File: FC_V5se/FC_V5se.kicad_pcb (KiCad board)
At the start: 4 copper layers, 88 x 94.5 mm, 220 parts, among them IC3 RV-3028-C7_32.768kHz_1ppm_TA_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, IC6 LT3652IMSE#PBF, J10 INHIBIT_P2, J11 DF11CZ-12DP-2V(27), J12 USB_C_Receptacle_USB2.0_16P, J14 Battery Input, J16 DEBUG, J17 Face4 (Z- Face), J18 Payload, J19 ISS_INHIBIT, J2 DF11CZ-12DP-2V(27), J20 RBF_Inhibit, J21 Heater Output, J22 SWD Port, J23 Aux Deploy 1, J24 Deploy 2, J29 INHIBIT_S2, J3 Life Makes Lemonade, J4 Conn_01x02, J5 BM04B-SRSS-TB(LF)(SN), J7 INHIBIT_P1, J8 INHIBIT_S1, SW1 KMR2, SW2 KMR2, U1 TLV1704, U10 TPS54226PWPRPWP14_2P31X2P46-L, U12 LT8610ABEMSE#TRPBF, U13 E22-400M30S, U14 TCA4307DGKR, U15 LIS2MDL, U16 INA219AxDCN, U19 AP22653AW6-7, U2 ZDSD04GLGEAG, U21 AP22653AW6-7, U22 AP22653AW6-7, U23 AP22653AW6-7, U24 AP22653AW6-7, U25 TPS2HB50AQPWPRQ1, U27 AP22653AW6-7, U29 AP22653AW6-7, U3 TCA9548APWR, U30 E28-2G4M27S, U6 TPS4H160AQPWPRQ1, U7 LSM6DSOTR, U8 INA219AxDCN

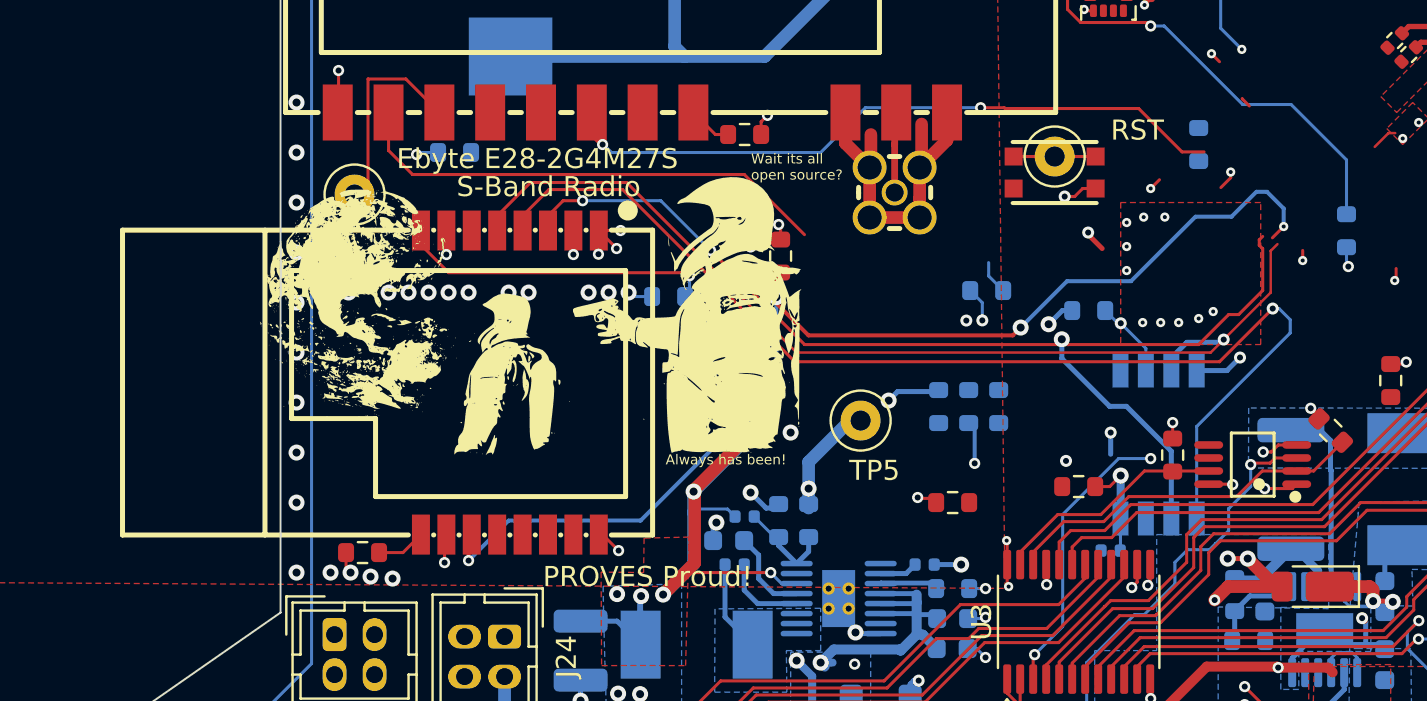
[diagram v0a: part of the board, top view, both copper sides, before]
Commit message: V5se: Deleted E28 S-Band Radio
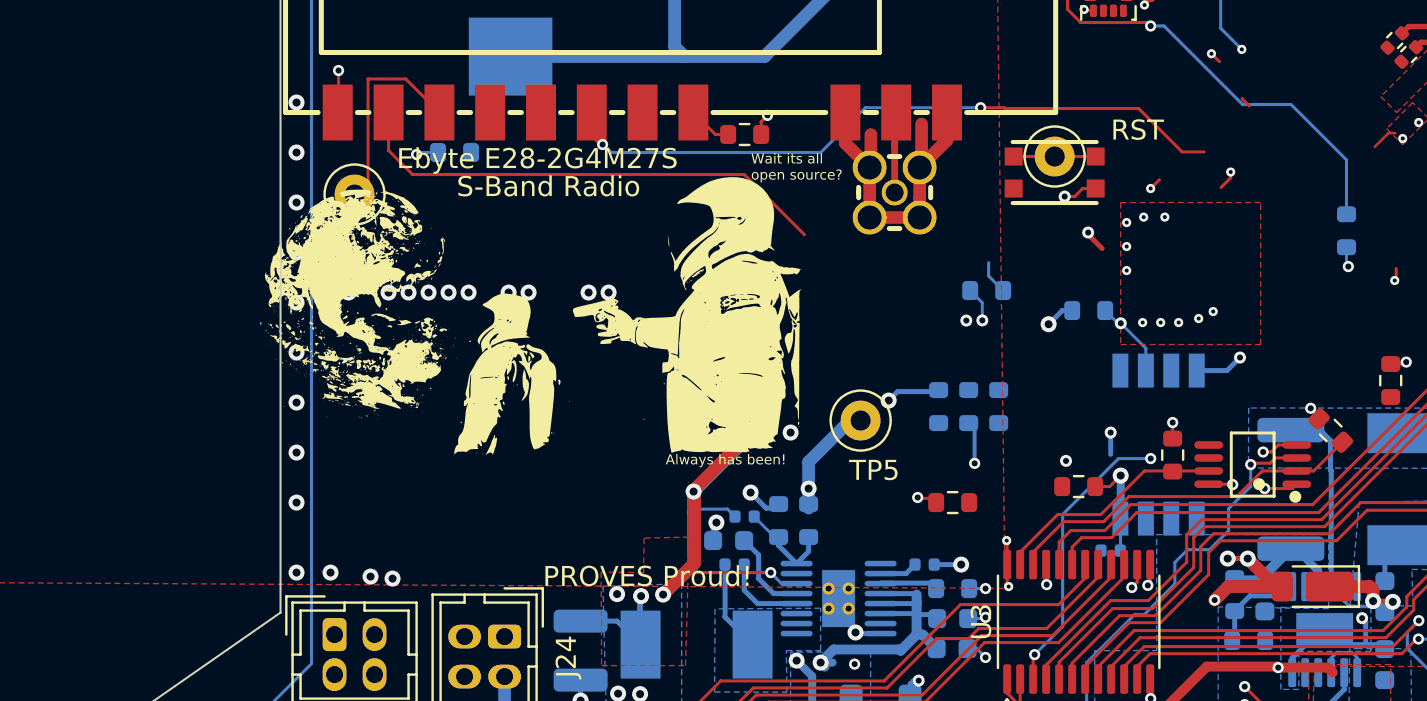
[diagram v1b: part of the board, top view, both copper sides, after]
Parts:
- removed R90: 10k, Resistor_SMD:R_0603_1608Metric
- removed R92, R95, R96: 100k, Resistor_SMD:R_0603_1608Metric
- removed U30: E28-2G4M27S, easyeda2kicad:WIRELM-SMD_E28-2G4M2XS
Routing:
- net SPI1_MOSI: track 60.0 -> 0.00 mm, vias 2 -> 0
- net RF2_RST: track 57.1 -> 0.00 mm, vias 4 -> 0
- net SPI1_MISO: track 55.9 -> 0.00 mm, vias 3 -> 0
- net SPI1_SCK: track 50.4 -> 0.00 mm, vias 1 -> 0
- net RF2_RX_EN: track 30.4 -> 0.00 mm, vias 1 -> 0
- net GND: track 225.2 -> 217.7 mm, vias 143 -> 137
- net +3V3: track 133.6 -> 129.2 mm, vias 57 -> 53
- net RF2_TX_EN: track 2.47 -> 0.00 mm
